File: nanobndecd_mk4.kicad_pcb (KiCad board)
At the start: 2 copper layers, 100 x 80 mm, 59 parts, among them CON1 5,5/2,1mm, J1 RJ45, J2 RJ45, J3 DB9, P1 CONN_01X16, P2 CONN_01X16, P3 CONN_02X08, P4 CONN_01X04, Q1 BS170, Q2 BS170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

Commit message: Corrected U1 footprint
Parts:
- C3: footprint Capacitors_SMD:C_1206_HandSoldering -> Capacitors_SMD:C_1812_HandSoldering
- U1: footprint Transistors_TO-220:TO-220_Neutral123_Vertical_MountedFromLS_LargePads -> Transistors_TO-220:TO-220_Neutral123_Vertical_LargePads
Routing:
- net +5VD: track 28.5 -> 37.7 mm
- net VCC: track 135.2 -> 134.2 mm, vias 1 -> 2

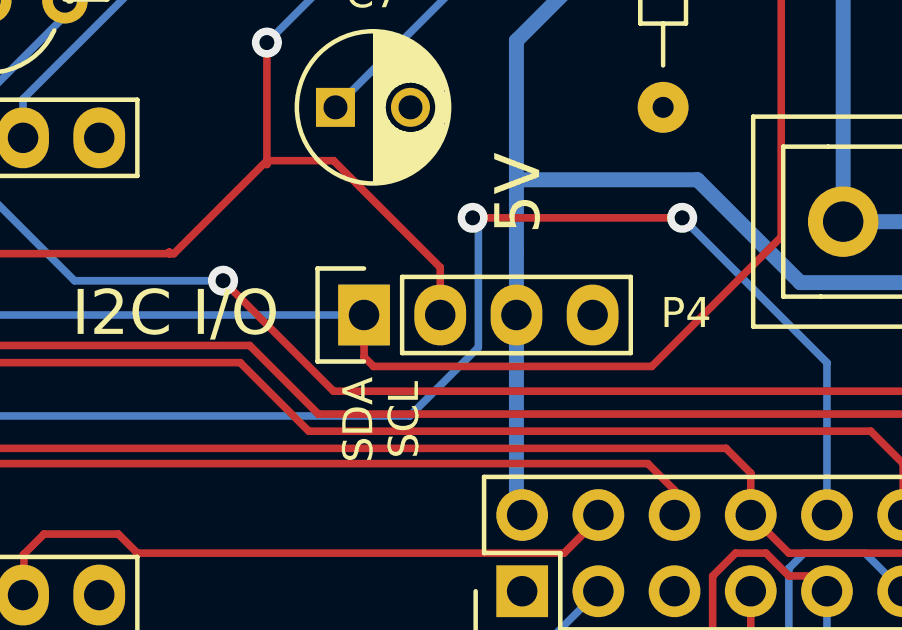
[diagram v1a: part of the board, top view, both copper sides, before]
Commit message: Corrected P4 to pin header
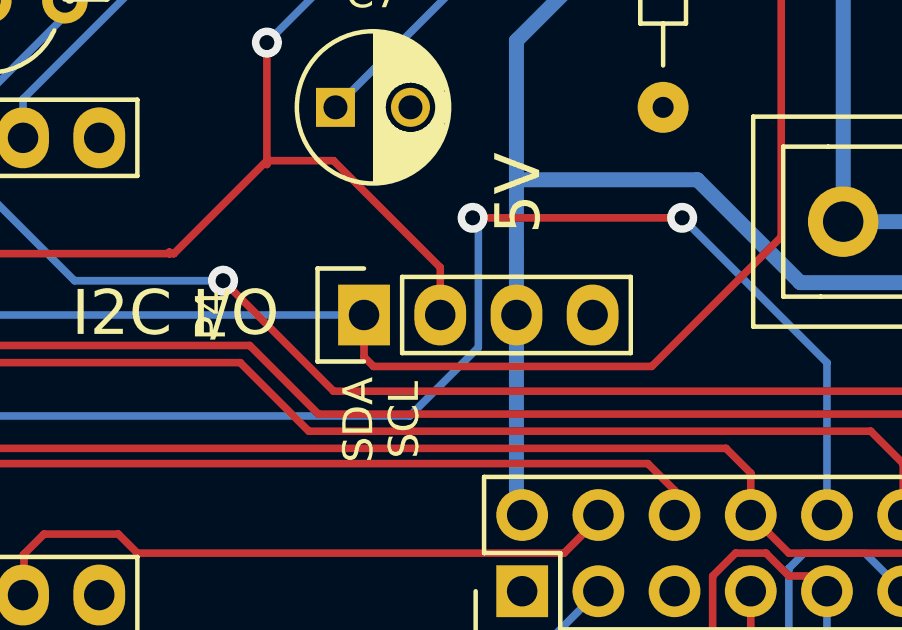
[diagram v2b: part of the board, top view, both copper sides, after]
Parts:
- P4: footprint Socket_Strips:Socket_Strip_Straight_1x04 -> Pin_Headers:Pin_Header_Straight_1x04
- turned P4 to 90 degrees
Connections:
- CON1 pad 3: (no net) -> Net-(CON1-Pad3)
- J1 pad 1: (no net) -> Net-(J1-Pad1)
- J1 pad 2: (no net) -> Net-(J1-Pad2)
- J1 pad 7: (no net) -> Net-(J1-Pad7)
- J1 pad 8: (no net) -> Net-(J1-Pad8)
- J3 pad 4: (no net) -> Net-(J3-Pad4)
- J3 pad 9: (no net) -> Net-(J3-Pad9)
- P1 pad 16: (no net) -> Net-(P1-Pad16)
- P1 pad 3: (no net) -> Net-(P1-Pad3)
- P2 pad 13: (no net) -> Net-(P2-Pad13)
- P2 pad 14: (no net) -> Net-(P2-Pad14)
- P2 pad 16: (no net) -> Net-(P2-Pad16)
- P2 pad 3: (no net) -> Net-(P2-Pad3)
- U2 pad 10: (no net) -> Net-(U2-Pad10)
- U2 pad 7: (no net) -> Net-(U2-Pad7)
- U2 pad 8: (no net) -> Net-(U2-Pad8)
- U2 pad 9: (no net) -> Net-(U2-Pad9)

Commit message: pcb text update
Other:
- board text added: "TS-590S(G) Arduino based Band Decoder Julho 2015"
- board text removed: "TS-590S(G) Arduino based Band Decoder Junho 2015"
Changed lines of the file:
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@@
-(kicad_pcb (version 4) (host pcbnew no-vcs-found-product)
+(kicad_pcb (version 4) (host pcbnew "(2015-06-24 BZR 5815)-product")
   (general
     (links 139)
@@
     (effects (font (size 1.3 1.3) (thickness 0.3)))
   )
-  (gr_text "TS-590S(G) Arduino based Band Decoder\nJunho 2015" (at 186.436 108.712) (layer B.SilkS)
+  (gr_text "TS-590S(G) Arduino based Band Decoder\nJulho 2015" (at 96.266 53.213 90) (layer B.SilkS)
     (effects (font (size 1.5 1.5) (thickness 0.3)) (justify left mirror))
   )
